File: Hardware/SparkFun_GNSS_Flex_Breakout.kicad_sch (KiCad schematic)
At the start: 51 parts, among them J1 microSD_Friction, J11 Conn_02x10, J12 Conn_02x10, U2 CH342F, U3 74HC4066BQ, U5 74HC4066BQ

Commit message: Update QFN-14 3D model. Nudge USB connectors
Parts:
- U3, U5: footprint SparkFun-Semiconductor-Standard:QFN-14_2.5x3mm_P0.5mm -> SparkFun-Semiconductor-Standard:QFN-14_2.5x3mm_P0.5mm_EP1x1.5mm
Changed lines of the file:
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@@
 			)
 		)
-		(property "Footprint" "SparkFun-Semiconductor-Standard:QFN-14_2.5x3mm_P0.5mm"
+		(property "Footprint" "SparkFun-Semiconductor-Standard:QFN-14_2.5x3mm_P0.5mm_EP1x1.5mm"
 			(at 191.77 123.19 0)
 			(effects
@@
 			)
 		)
-		(property "Footprint" "SparkFun-Semiconductor-Standard:QFN-14_2.5x3mm_P0.5mm"
+		(property "Footprint" "SparkFun-Semiconductor-Standard:QFN-14_2.5x3mm_P0.5mm_EP1x1.5mm"
 			(at 191.77 74.93 0)
 			(effects

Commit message: Routing WIP
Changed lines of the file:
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@@
 	(title_block
 		(title "SparkFun GNSS Flex Breakout")
-		(date "2025-03-28")
+		(date "2025-04-03")
 		(rev "v01")
 		(company "SparkFun Electronics")
@@
 	)
 	(global_label "SD_DAT3"
-		(shape output)
+		(shape bidirectional)
 		(at 99.06 63.5 0)
 		(fields_autoplaced yes)
@@
 		)
 		(property "Intersheetrefs" "${INTERSHEET_REFS}"
-			(at 110.028 63.5 0)
+			(at 111.1393 63.5 0)
 			(effects
 				(font
@@
 	)
 	(global_label "SD_DAT3"
-		(shape input)
+		(shape bidirectional)
 		(at 27.94 171.45 180)
 		(fields_autoplaced yes)
@@
 		)
 		(property "Intersheetrefs" "${INTERSHEET_REFS}"
-			(at 16.972 171.45 0)
+			(at 15.8607 171.45 0)
 			(effects
 				(font
@@
 	)
 	(global_label "SD_CMD"
-		(shape output)
+		(shape bidirectional)
 		(at 99.06 55.88 0)
 		(fields_autoplaced yes)
@@
 		)
 		(property "Intersheetrefs" "${INTERSHEET_REFS}"
-			(at 109.4837 55.88 0)
+			(at 110.595 55.88 0)
 			(effects
 				(font
@@
 	)
 	(global_label "SD_CMD"
-		(shape input)
+		(shape bidirectional)
 		(at 27.94 184.15 180)
 		(fields_autoplaced yes)
@@
 		)
 		(property "Intersheetrefs" "${INTERSHEET_REFS}"
-			(at 17.5163 184.15 0)
+			(at 16.405 184.15 0)
 			(effects
 				(font
@@
 	)
 	(global_label "SD_DAT0"
-		(shape input)
+		(shape bidirectional)
 		(at 27.94 179.07 180)
 		(fields_autoplaced yes)
@@
 		)
 		(property "Intersheetrefs" "${INTERSHEET_REFS}"
-			(at 16.972 179.07 0)
+			(at 15.8607 179.07 0)
 			(effects
 				(font
@@
 	)
 	(global_label "SD_DAT0"
-		(shape output)
+		(shape bidirectional)
 		(at 99.06 60.96 0)
 		(fields_autoplaced yes)
@@
 		)
 		(property "Intersheetrefs" "${INTERSHEET_REFS}"
-			(at 110.028 60.96 0)
-			(effects
-				(font
+			(at 111.1393 60.96 0)
+			(effects
+				(font

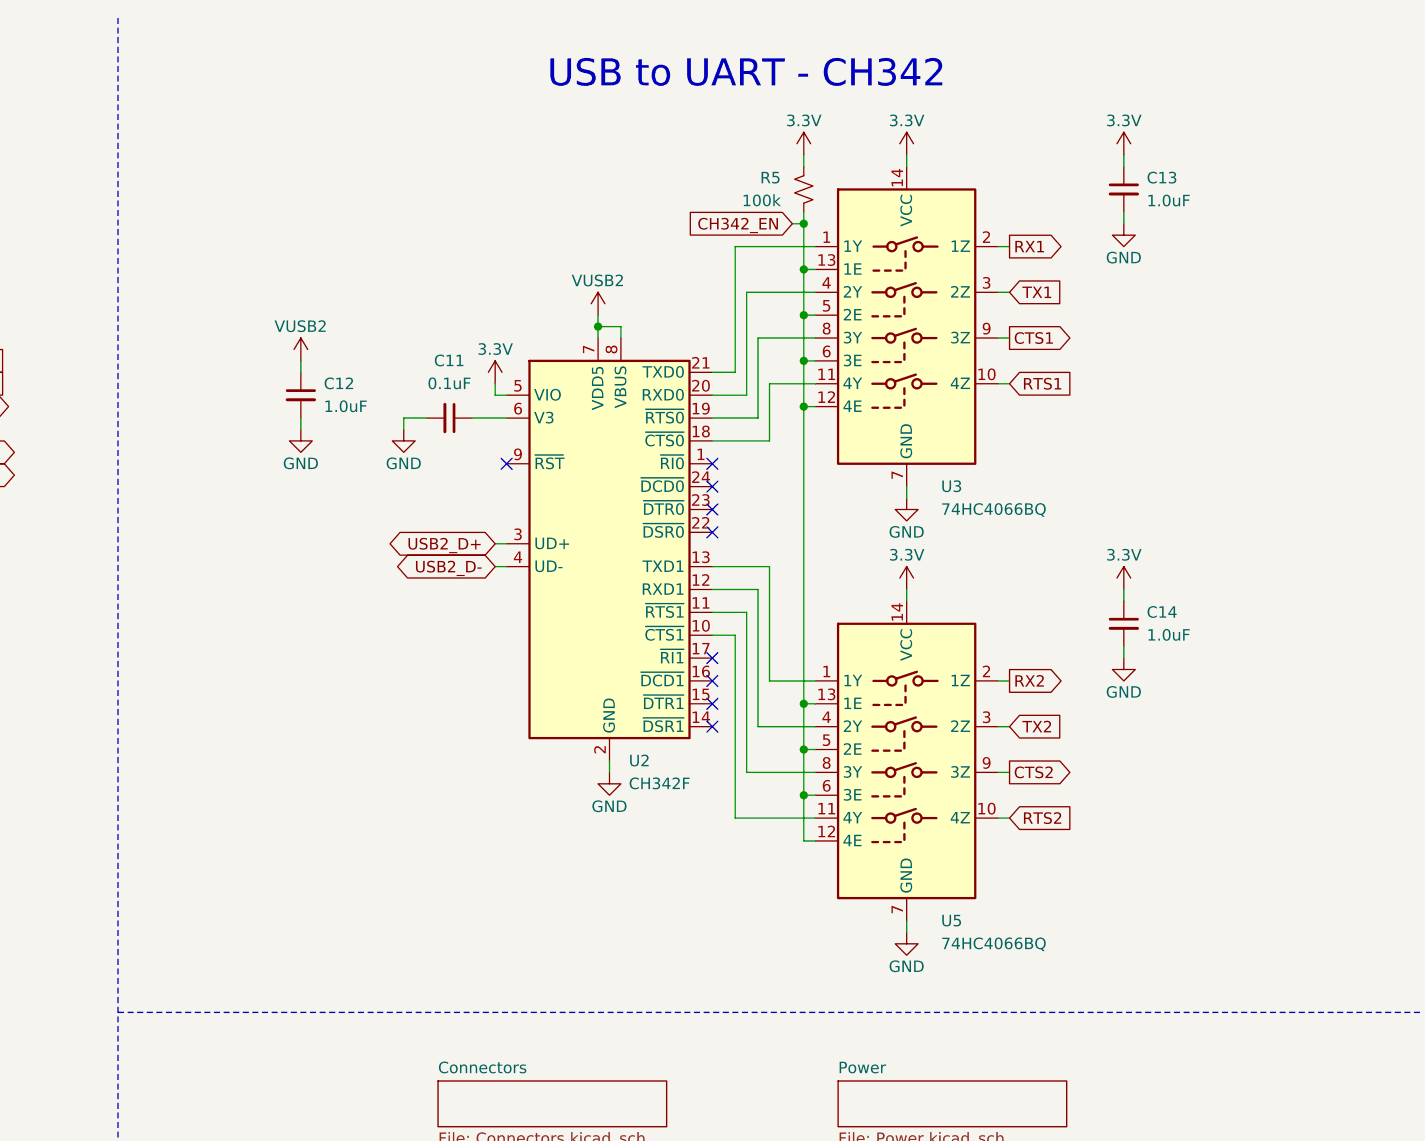
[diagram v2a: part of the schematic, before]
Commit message: Routed and panelized
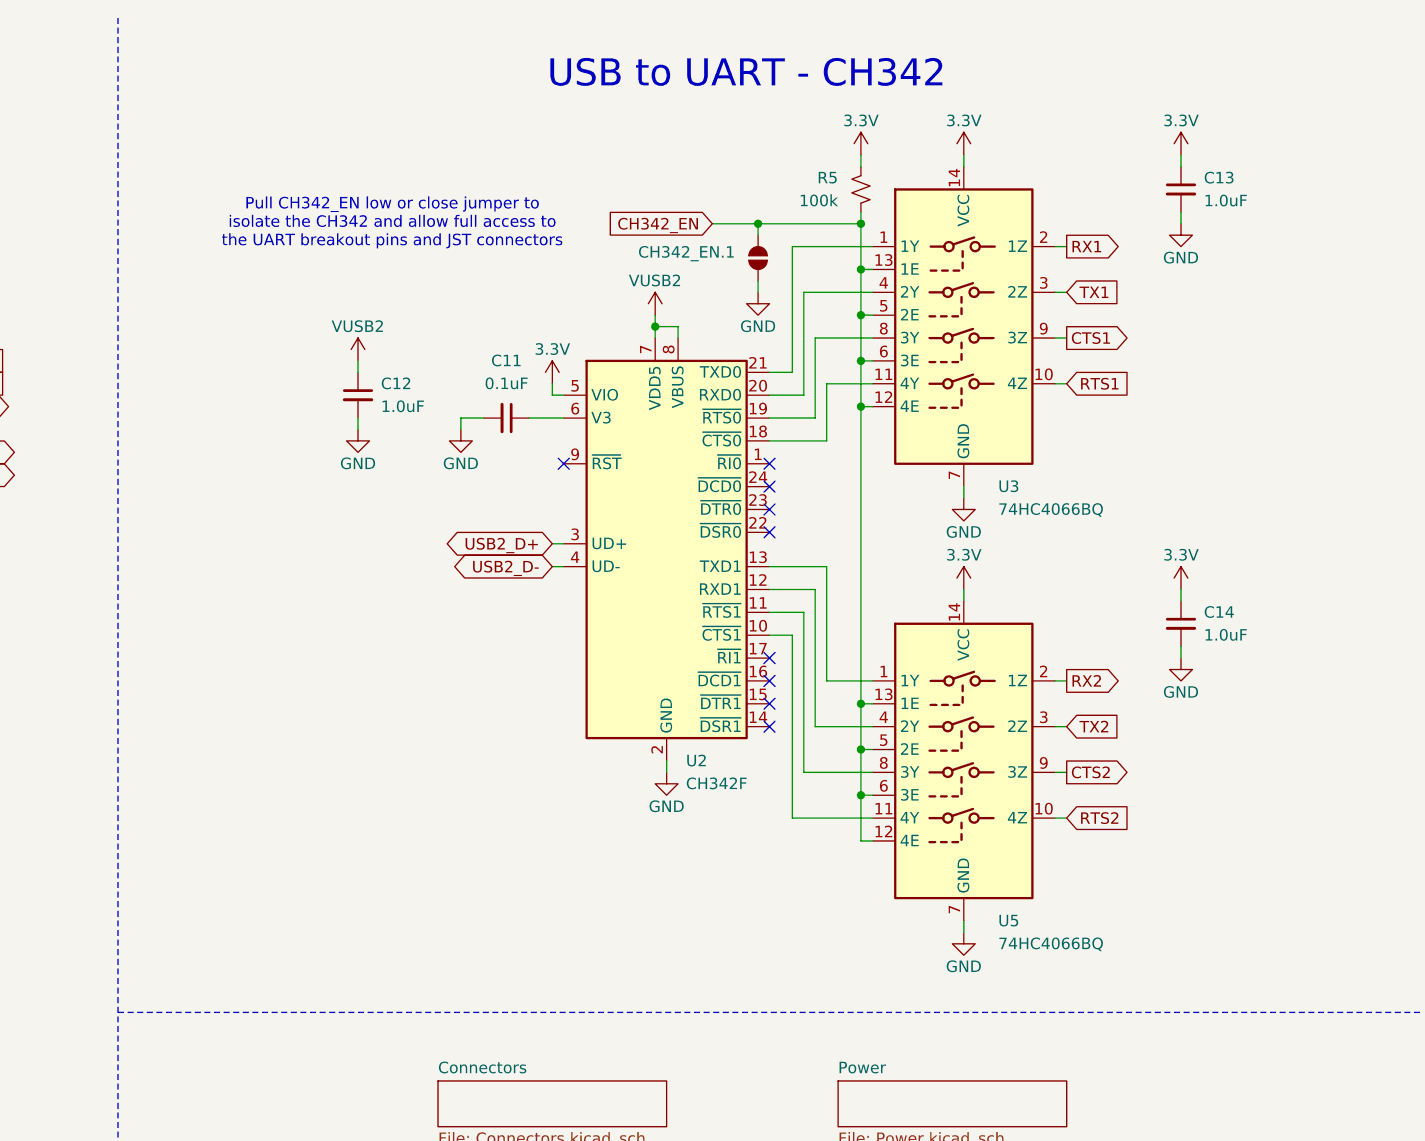
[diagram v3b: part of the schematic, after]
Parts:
- added CH342_EN.1: ~, SparkFun-Jumper:Jumper_2_NO, symbol SparkFun-Jumper:SolderJumper_2_Open
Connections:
- net CH342_EN: now also CH342_EN.1.2 (B)
- net GND: now also CH342_EN.1.1 (A)
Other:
- note added: "Pull CH342_EN low or close jumper to isolate the CH342 and allow full access to the UART breakout pins and JST connectors"
- moved on the sheet: C11, C12, C13, C14, R5, U2, U3, U5

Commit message: Updates after proto review
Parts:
- added J15: Legend: GNSS Flex, SparkFun-Aesthetic:GNSS_Flex_Template, symbol SparkFun-Aesthetic:GNSS_Flex_Module_Legend
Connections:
- net VBATT renamed VBACKUP
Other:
- note added: "GNSS Flex Module"
- note removed: "Flex GNSS Module"
- moved on the sheet: C1, C10, C2, C4, C5, C6, J11, J12

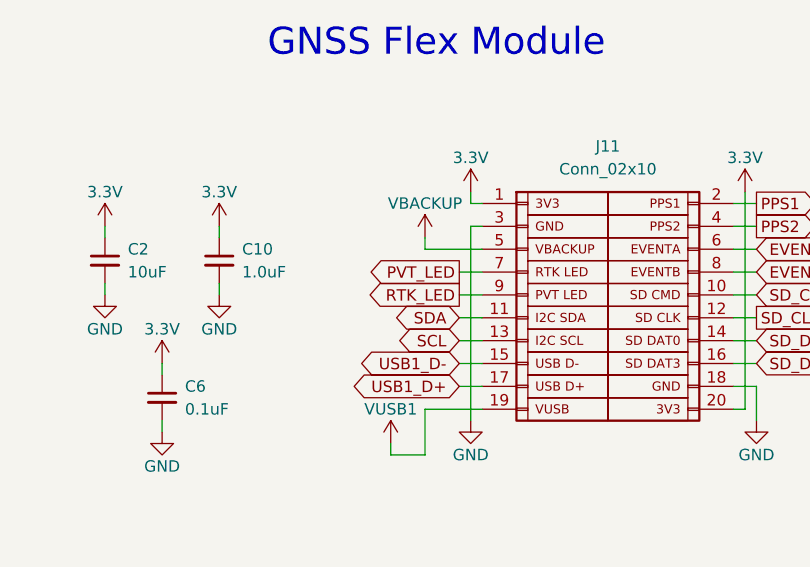
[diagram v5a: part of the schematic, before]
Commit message: v10 PCB - correct PVT and RTK LEDs, and VBACKUP silk
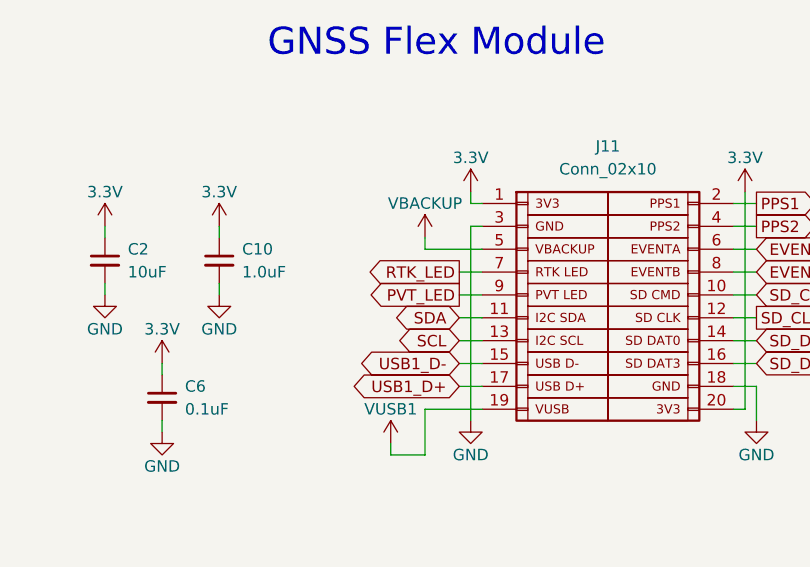
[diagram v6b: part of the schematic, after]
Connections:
- net PVT_LED: now also J11.9 (Pin_9); no longer J11.7 (Pin_7)
- net RTK_LED: now also J11.7 (Pin_7); no longer J11.9 (Pin_9)
